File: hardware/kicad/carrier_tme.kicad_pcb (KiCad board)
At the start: 2 copper layers, 90 x 60 mm, 65 parts, among them J2 Heltec_J2, J3 Heltec_J3, U2 TCA9534PWR

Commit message: hardware: UART debug header on all boards, I2C header and rail test pads on carrier, SDA/SCL pads on pack
Header is 1x3 2.54 mm (GND, MCU TX, MCU RX), hand-soldered, kept out of the BOM.
Carrier uses Heltec UART0 (GPIO43/44), STM32 boards USART1 (PA9/PA10).

Co-Authored-By: Claude Sonnet 5.5 <noreply@anthropic.com>
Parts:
- added J_I2C1: I2C, Connector_PinHeader_2.54mm:PinHeader_1x04_P2.54mm_Vertical, F.Cu at (56.0, 55.5)
- added J_UART1: UART, Connector_PinHeader_2.54mm:PinHeader_1x03_P2.54mm_Vertical, F.Cu at (47.0, 55.5)
- added TP_3V3: 3V3, TestPoint:TestPoint_Pad_D1.5mm, F.Cu at (68.0, 55.5)
- added TP_5V: 5V, TestPoint:TestPoint_Pad_D1.5mm, F.Cu at (70.5, 55.5)
- added TP_GND: GND, TestPoint:TestPoint_Pad_D1.5mm, F.Cu at (75.5, 55.5)
- added TP_VSW: VBAT_SW, TestPoint:TestPoint_Pad_D1.5mm, F.Cu at (73.0, 55.5)
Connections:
- J2 pad 5: unconnected-(J2-Pin_5-Pad5) -> UART_RX
- J2 pad 6: unconnected-(J2-Pin_6-Pad6) -> UART_TX
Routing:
- net SDA_3V3: track 95.4 -> 178.4 mm, vias 3 -> 2
- net VBAT_SW: track 52.5 -> 126.8 mm, vias 1 -> 2
- net +5V: track 139.7 -> 209.8 mm, vias 2 -> 1
- net SCL_3V3: track 124.1 -> 170.8 mm, vias 4 -> 2
- net GND: track 348.9 -> 386.3 mm, vias 12 -> 10
- net LED_B_G: track 45.2 -> 81.6 mm, vias 2 -> 6
- net +3V3: track 186.2 -> 219.3 mm, vias 8 -> 7
- net DAC_OR: track 31.0 -> 53.9 mm
- net AMP_SD: track 82.0 -> 63.9 mm, vias 2 -> 4
- net DAC_OL: track 49.3 -> 31.7 mm, vias 2 -> 4
- net UART_TX: track 0.00 -> 12.5 mm
- net AUD_R: track 58.2 -> 48.4 mm
- net EXP_INT: track 25.6 -> 33.8 mm
- net AUD_L: track 60.8 -> 68.9 mm
- net AMP_INP: track 26.9 -> 19.2 mm, vias 2 -> 0
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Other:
- board text added: "3V3"
- board text added: "5V"
- board text added: "GND"
- board text added: "I2C GND 3V3 SDA SCL"
- board text added: "UART GND TX RX"
- board text added: "VSW"

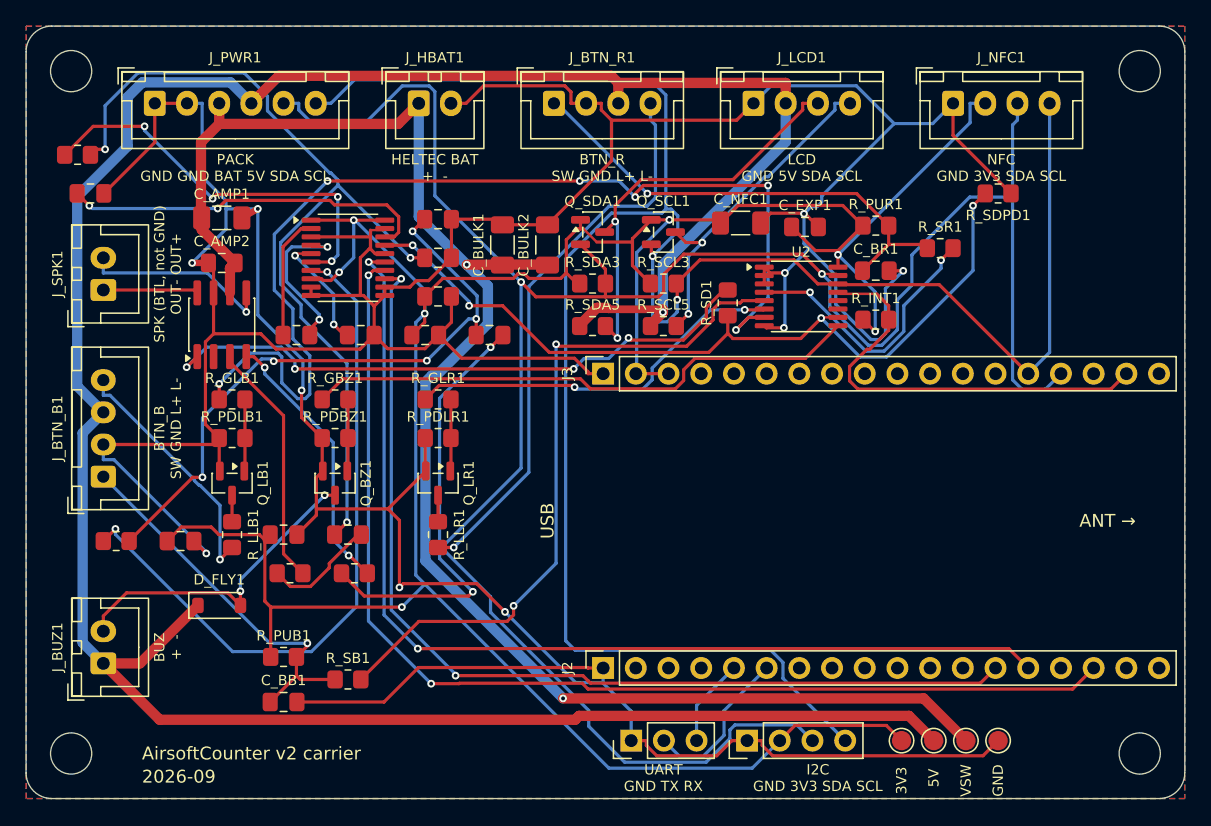
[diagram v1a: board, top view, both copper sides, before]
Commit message: hardware: KiCad 10 pipeline fixes, +5V reservoir caps, NS4168 1uF, pack UART header off the holders
KiCad 9 -> 10.0.7 broke the generators even on HEAD:
- gen_sch: libraries moved (hide yes) from effects to the property; read both,
  write it back into effects (KiCad 9 format), so hidden fields stop showing
  on every sheet and stop blocking the schematic router. Add the title block.
- gen_pcb: SetDoNotAllowCopperPour -> SetDoNotAllowZoneFills; copy the symbol's
  Datasheet/Description/Sim fields onto footprints (schematic parity now fails
  DRC); refuse THT pads under bottom-side parts (PTH_UNDER_OK allowlist).
- route.py: Power class routed at +40 um (Freerouting's octagons undercut 0.8 mm
  round ends, KiCad 10 exports no clearance margin), falling back to no margin
  if that leaves a connection unrouted; strip dangling stubs after SES import.
- pack: USB-C shield pin S1 -> SH; pack_tme: VSSOP-10 -> MSOP-10 footprint.

Design changes from the Konnect MCP review and datasheet check:
- carrier: C_5V1 10 uF + C_5V2 100 nF on +5V at J_PWR1 (no local cap before);
  C_AMP2 100 nF -> 1 uF per NS4168 datasheet (100 uF || 1 uF). carrier_tme
  places the new caps clear of its DAC.
- pack/pack_tme: J_UART1 sat under BT4 (bottom-side 18650 holder), caught by
  KiCad 10's pth_inside_courtyard; moved to the right strip, label in pin order.
  The NTC beads stay in the holder window (check ignored, gen_pcb enforces it).
- Docs: ORDERING counts, NS4168/TCA9534/BSS138/1N4148W datasheet check,
  TCA9534 P6/P7 firmware note.

All six boards: ERC 0, DRC 0 (0 unconnected, 0 parity), gerbers ok.

Co-Authored-By: Claude Opus 5.5 <noreply@anthropic.com>
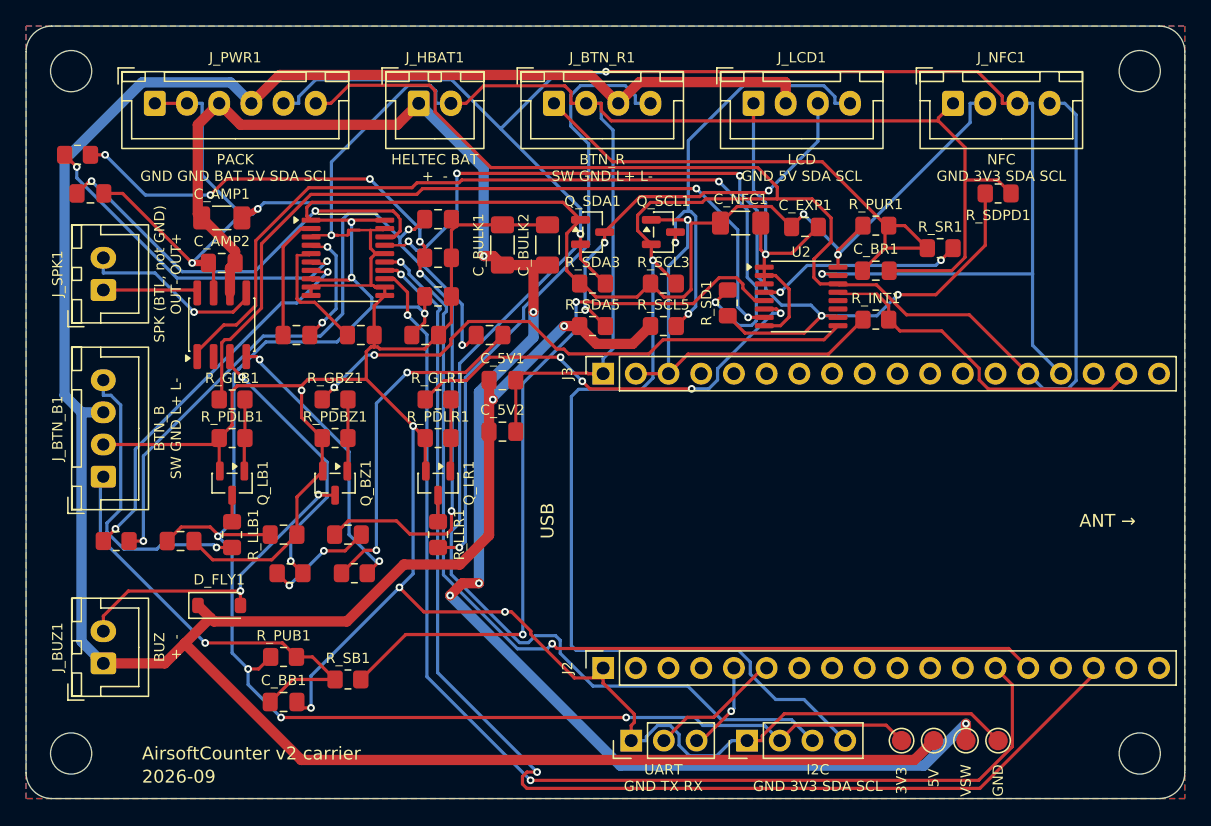
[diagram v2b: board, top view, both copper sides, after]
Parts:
- added C_5V1: 10uF, Capacitor_SMD:C_0805_2012Metric_Pad1.18x1.45mm_HandSolder, F.Cu at (37.0, 27.5)
- added C_5V2: 100nF, Capacitor_SMD:C_0805_2012Metric_Pad1.18x1.45mm_HandSolder, F.Cu at (37.0, 31.5)
- C_AMP2: value 100nF -> 1uF
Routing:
- net DAC_OR: track 53.9 -> 30.2 mm
- net +3V3: track 219.3 -> 242.4 mm, vias 7 -> 10
- net +5V: track 209.8 -> 231.8 mm, vias 1 -> 2
- net LED_B_G: track 81.6 -> 62.2 mm, vias 6 -> 2
- net AMP_SD_R: track 48.1 -> 66.9 mm, vias 4 -> 2
- net AMP_SD: track 63.9 -> 76.1 mm, vias 4 -> 5
- net I2S_BCLK: track 77.2 -> 89.2 mm
- net SCL_5V: track 26.2 -> 34.4 mm
- net I2S_DIN: track 87.5 -> 95.3 mm
- net GND: track 386.3 -> 378.7 mm, vias 10 -> 9
- net AMP_INN_C: track 34.1 -> 26.9 mm
- net EXP_INT: track 33.8 -> 27.2 mm
- net AUD_R: track 48.4 -> 54.9 mm, vias 5 -> 3
- net SCL_3V3: track 170.8 -> 177.1 mm, vias 2 -> 1
- net SDA_3V3: track 178.4 -> 184.0 mm, vias 2 -> 3
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
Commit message: hardware: TME cost cuts (3 fewer resistor tapes, leaner spares); route.py survives KiCad 10's SWIG break
carrier_tme: R_OL/R_OR 470R -> 1k (DAC RC corner 72 kHz), R_LLB1/R_LLR1 0R -> 10R (button LEDs
have their own resistors). pack_xiao: R_GS1..4 1M -> 240k (17 uA per closed switch). Drops the
0805 0R, 470R and 1M tapes. tme_all: 1206 caps and the 0603 NTC get +10 % spares, no minimum 5.
About -44 PLN on the 5+5 order (order_35742850 prices).

route.py: stub_free moves from --finish to --import. Its connectivity rebuilds broke the SWIG type
table for the rest of the process, so finish() got bare SwigPyObjects for zones (carrier_tme
segfaulted in apport's excepthook on the AttributeError). Placement unchanged on both boards.

Co-Authored-By: Claude Opus 5.5 <noreply@anthropic.com>
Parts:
- R_LLB1, R_LLR1: value 0R -> 10R
- R_OL, R_OR: value 470R -> 1k
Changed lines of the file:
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@@
 			)
 		)
-		(property "Value" "470R"
+		(property "Value" "1k"
 			(at 0 1.65 0)
 			(layer "F.Fab")
@@
 			)
 		)
-		(property "Value" "0R"
+		(property "Value" "10R"
 			(at 0 1.65 270)
 			(layer "F.Fab")
@@
 			)
 		)
-		(property "Value" "0R"
+		(property "Value" "10R"
 			(at 0 1.65 270)
 			(layer "F.Fab")
@@
 			)
 		)
-		(property "Value" "470R"
+		(property "Value" "1k"
 			(at 0 1.65 0)
 			(layer "F.Fab")

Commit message: hardware: 3.5" ILI9488 SPI TFT replaces the Newhaven LCD
Carrier and carrier_tme: J_LCD1 XH-8 (VCC GND CS RST DC MOSI SCK LED,
the module header order; CS tied low). SPI3 on GPIO43/44, PWM backlight
on GPIO6 (R_BLPD1), DC/RST on TCA9534 P6/P7, buttons polled. The P4/P5
native-pin option was dropped: the Heltec GNSS receptacle opens toward
those pins. Removed the I2C level shifter, R_INT1/EXP_INT and J_UART1;
J_NFC1 moved to the bottom edge. Both boards: 0 unrouted, ERC/DRC/parity 0.

Lid rebuilt from the LCDWiki MSP3520 drawing: 98 x 56.34, M3 bosses on
92 x 49.5 (r3.0, 4.5 high), 80 x 51 viewing window, 11.5 mm depth.
make mech green. Power model: backlight duty is now the mean PWM level.

Co-Authored-By: Claude Opus 5.5 <noreply@anthropic.com>
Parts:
- removed J_UART1: UART, Connector_PinHeader_2.54mm:PinHeader_1x03_P2.54mm_Vertical
- removed Q_SCL1, Q_SDA1: BSS138, Package_TO_SOT_SMD:SOT-23
- removed R_INT1: 10k, Resistor_SMD:R_0805_2012Metric_Pad1.20x1.40mm_HandSolder
- removed R_SCL5, R_SDA5: 4k7, Resistor_SMD:R_0805_2012Metric_Pad1.20x1.40mm_HandSolder
- added R_BLPD1: 10k, Resistor_SMD:R_0805_2012Metric_Pad1.20x1.40mm_HandSolder, F.Cu at (66.0, 22.8)
- J_LCD1: footprint Connector_JST:JST_XH_B4B-XH-A_1x04_P2.50mm_Vertical -> Connector_JST:JST_XH_B8B-XH-A_1x08_P2.50mm_Vertical
- moved J_NFC1 53.9 mm to (51.0, 55.6), turned to 180 degrees
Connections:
- J2 pad 5: UART_RX -> LCD_MOSI
- J2 pad 6: UART_TX -> LCD_SCK
- J3 pad 17: EXP_INT -> LCD_BL
- J_LCD1 pad 1: GND -> +5V
- J_LCD1 pad 2: +5V -> GND
- J_LCD1 pad 3: SDA_5V -> GND
- J_LCD1 pad 4: SCL_5V -> LCD_RST
- U2 pad 11: unconnected-(U2-P6-Pad11) -> LCD_DC
- U2 pad 12: unconnected-(U2-P7-Pad12) -> LCD_RST
- U2 pad 13: EXP_INT -> unconnected-(U2-~{INT}-Pad13)
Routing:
- net LCD_SCK: track 0.00 -> 85.1 mm, vias 0 -> 2
- net LCD_MOSI: track 0.00 -> 78.3 mm, vias 0 -> 2
- net SDA_3V3: track 184.0 -> 134.6 mm
- net LCD_BL: track 0.00 -> 43.4 mm, vias 0 -> 1
- net SCL_3V3: track 177.1 -> 140.8 mm, vias 1 -> 4
- net SCL_5V: track 34.4 -> 0.00 mm, vias 2 -> 0
- net SDA_5V: track 31.2 -> 0.00 mm, vias 3 -> 0
- net +3V3: track 242.4 -> 212.0 mm, vias 10 -> 6
- net EXP_INT: track 27.2 -> 0.00 mm
- net +5V: track 231.8 -> 205.0 mm
- net LCD_DC: track 0.00 -> 23.7 mm, vias 0 -> 1
- net LCD_RST: track 0.00 -> 18.5 mm, vias 0 -> 1
- net DAC_OR: track 30.2 -> 43.4 mm
- net AMP_SD_R: track 66.9 -> 55.5 mm, vias 2 -> 4
- net UART_TX: track 10.3 -> 0.00 mm
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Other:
- board text added: "LCD 5V GND CS0 RST DC MOSI SCK BL"
- board text added: "NFC SCL SDA 3V3 GND"
- board text removed: "LCD GND 5V SDA SCL"
- board text removed: "NFC GND 3V3 SDA SCL"
- board text removed: "UART GND TX RX"
